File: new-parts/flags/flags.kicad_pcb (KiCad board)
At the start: 2 copper layers, 45.7 x 41.9 mm, 12 parts, among them J1 BHR-10-VUA, J2 Conn_02x03_Odd_Even, K1 J104D2C12VDC.15S

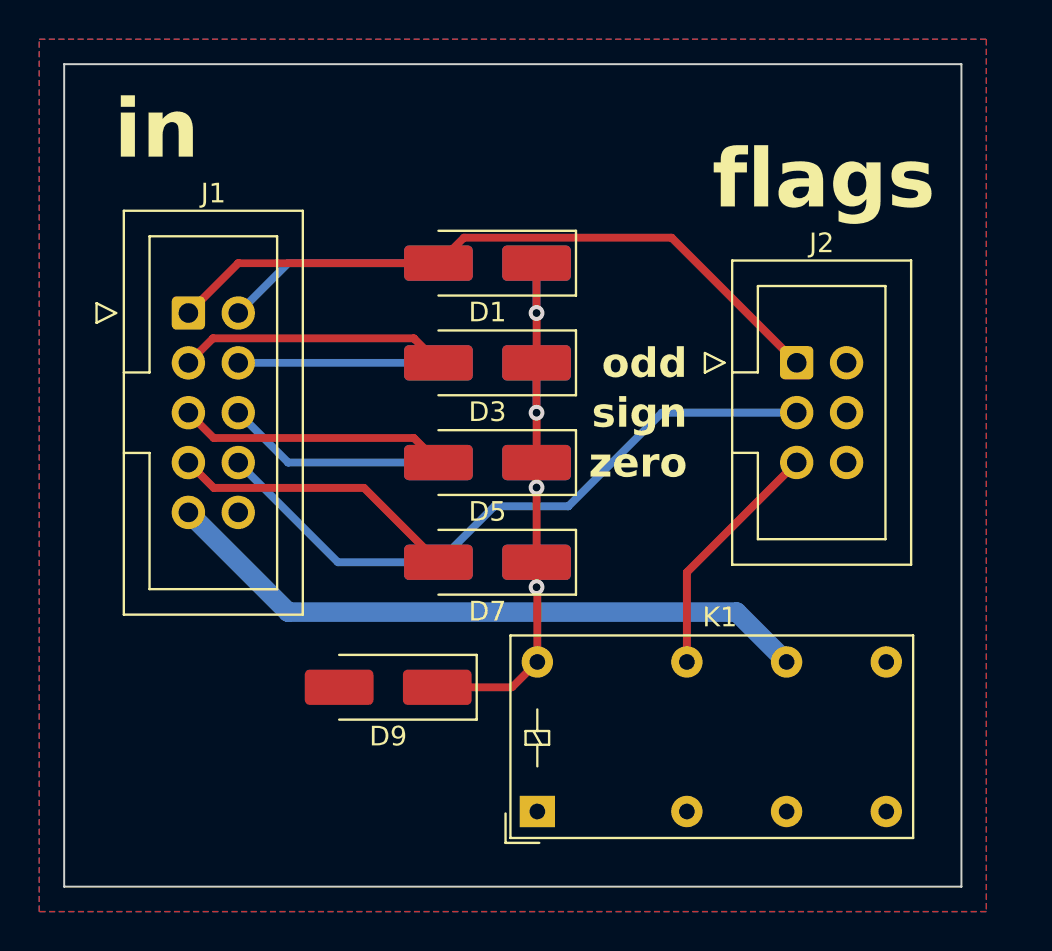
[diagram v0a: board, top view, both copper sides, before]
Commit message: Change all two-pin headers for control + ground to control only.
This is to prevent accidental short circuits when they are plugged in the
wrong way.
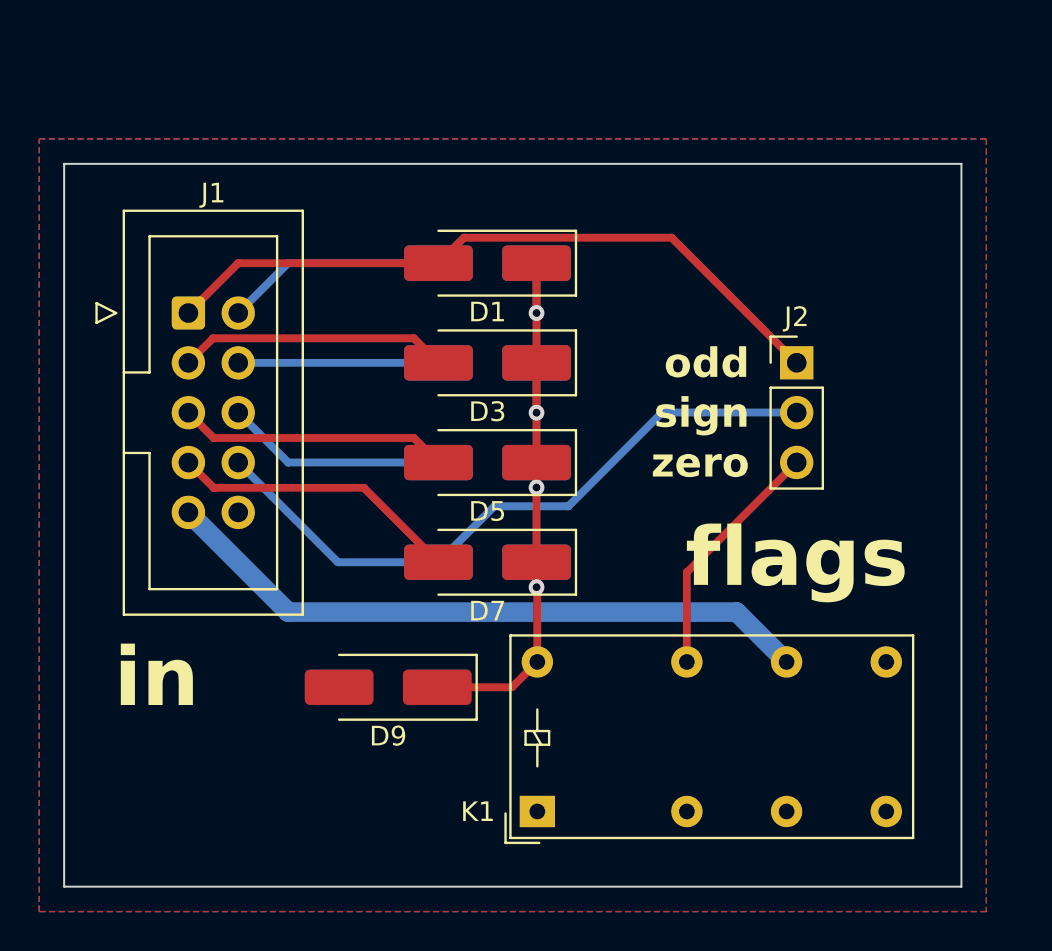
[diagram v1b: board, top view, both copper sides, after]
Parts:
- J2: footprint Connector_IDC:IDC-Header_2x03_P2.54mm_Vertical -> Connector_PinHeader_2.54mm:PinHeader_1x03_P2.54mm_Vertical
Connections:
- J2 pad 2: GND -> Net-(D8-A)
- J2 pad 3: Net-(D8-A) -> Net-(J2-Pin_3)
- K1 pad 21: Net-(J2-Pin_5) -> Net-(J2-Pin_3)
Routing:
- net Net-(J2-Pin_5): track 12.5 -> 0.00 mm
- net Net-(J2-Pin_3): track 0.00 -> 12.5 mm
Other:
- board size 45.7 x 41.9 mm -> 45.7 x 36.8 mm

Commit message: Add placeholders for JLC order number.
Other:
- board text added: "JLCJLCJLCJLC"
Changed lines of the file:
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@@
   (gr_line (start 167.64 71.12) (end 167.64 107.95)
     (stroke (width 0.1) (type default)) (layer "Edge.Cuts"))
+  (gr_text "JLCJLCJLCJLC" (at 166.116 106.934) (layer "B.SilkS")
+    (effects (font (size 1 1) (thickness 0.15)) (justify left bottom mirror))
+  )
   (gr_text "flags" (at 159.258 91.186) (layer "F.SilkS")
     (effects (font (size 3 3) (thickness 0.6) bold))

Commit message: Add a "title" label to all parts.
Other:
- board text added: "vis vitalis - flags"
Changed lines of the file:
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@@
   (gr_line (start 167.64 71.12) (end 167.64 107.95)
     (stroke (width 0.1) (type default)) (layer "Edge.Cuts"))
+  (gr_text "vis vitalis - flags" (at 166.116 102.108) (layer "B.SilkS")
+    (effects (font (size 3 3) (thickness 0.6) bold) (justify left bottom mirror))
+  )
   (gr_text "JLCJLCJLCJLC" (at 166.116 106.934) (layer "B.SilkS")
     (effects (font (size 1 1) (thickness 0.15)) (justify left bottom mirror))
